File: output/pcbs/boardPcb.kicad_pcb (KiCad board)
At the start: 2 copper layers, 188.6 x 119.9 mm, 118 parts

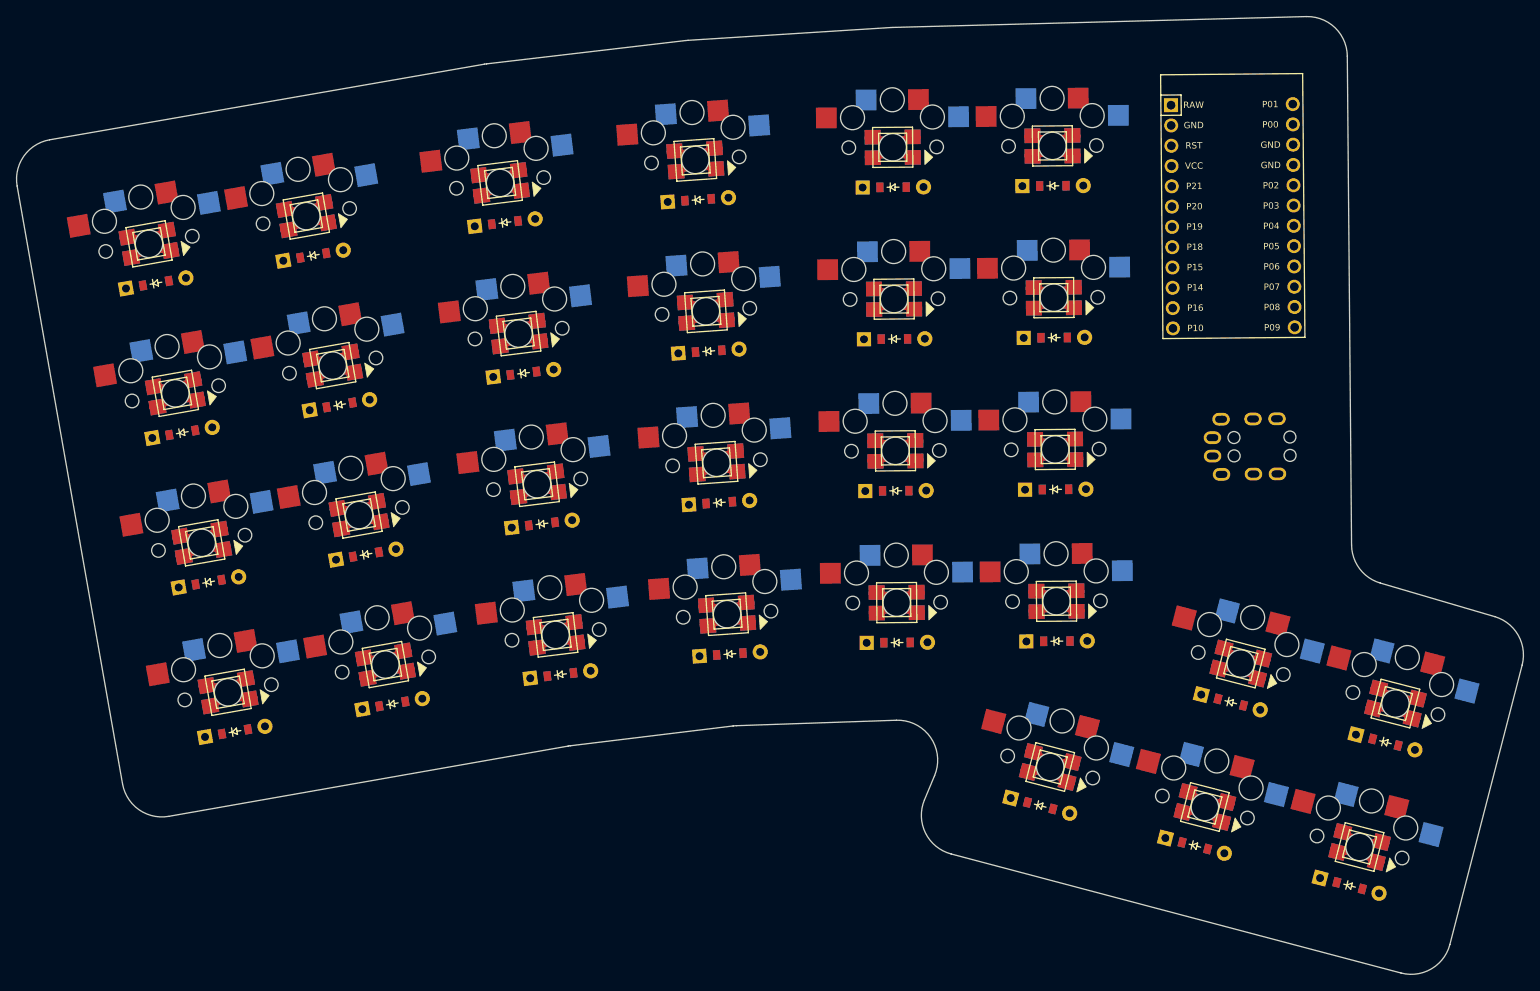
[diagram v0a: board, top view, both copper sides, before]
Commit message: created some PCB stuff; prep for layout
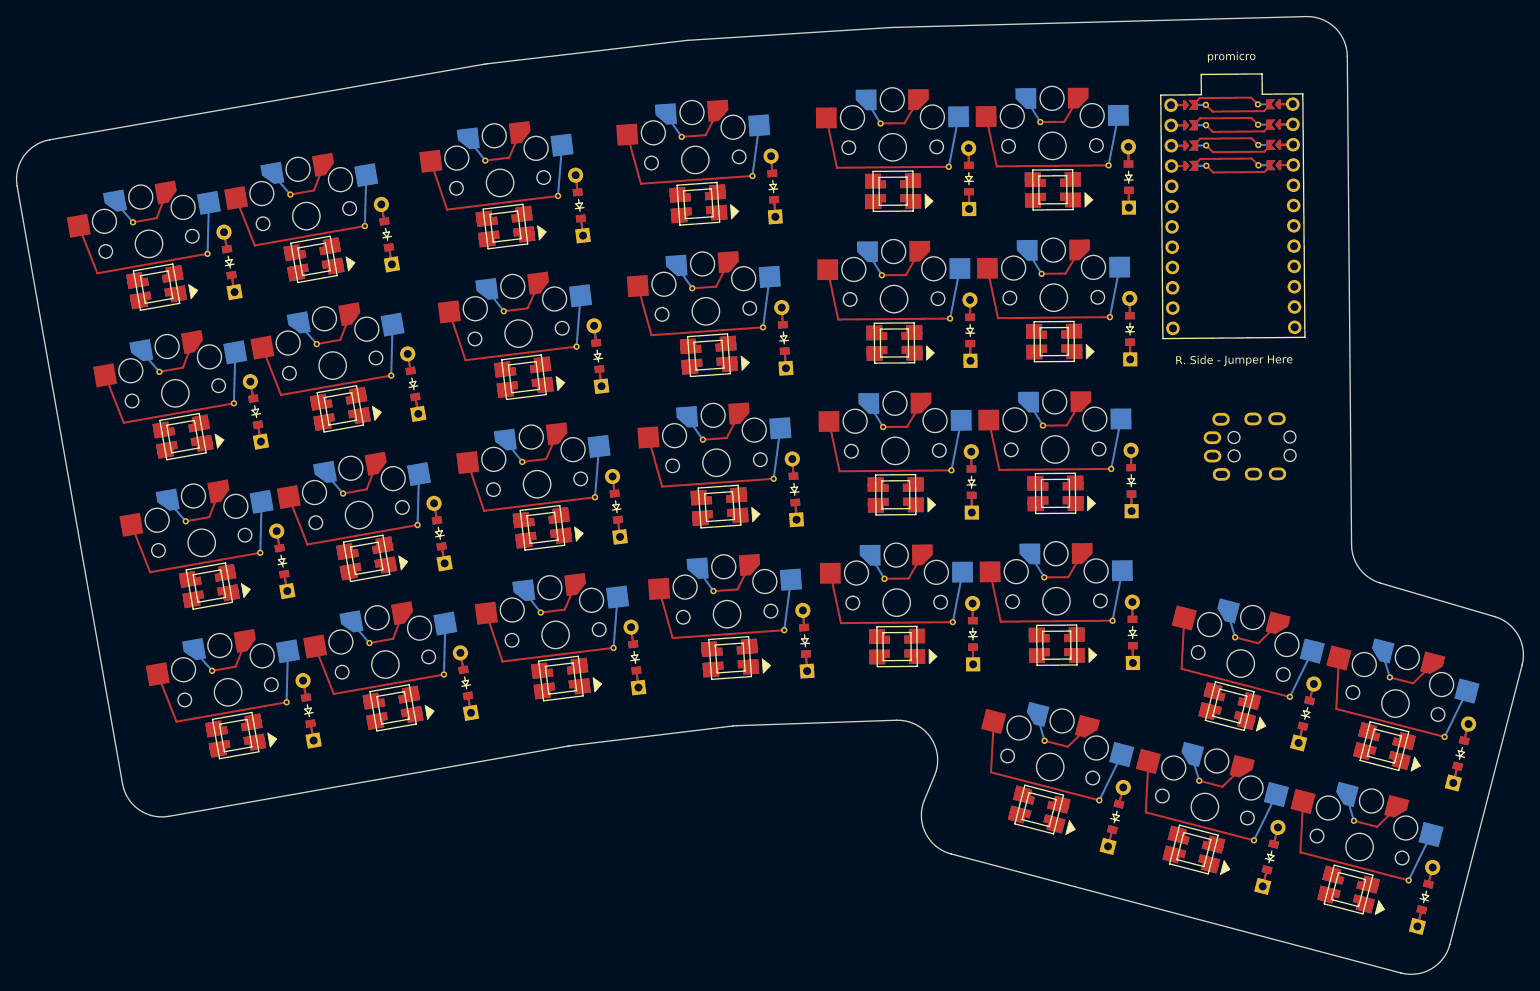
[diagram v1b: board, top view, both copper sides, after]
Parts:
- removed MCU1: , ProMicro
- added ?: , ProMicro, F.Cu at (258.8, 119.0)
- moved D1 9.55 mm to (143.1, 180.9), turned to 100 degrees
- moved D2 9.55 mm to (139.8, 162.2), turned to 100 degrees
- moved D4 9.55 mm to (133.2, 124.8), turned to 100 degrees
- moved D5 9.55 mm to (162.8, 177.4), turned to 100 degrees
- moved D6 9.55 mm to (159.5, 158.7), turned to 100 degrees
- moved D7 9.55 mm to (156.2, 140.0), turned to 100 degrees
- moved D8 9.55 mm to (152.9, 121.3), turned to 100 degrees
- moved D3 9.55 mm to (136.5, 143.5), turned to 100 degrees
- moved D10 9.55 mm to (181.6, 155.4), turned to 97 degrees
- moved D11 9.55 mm to (179.3, 136.5), turned to 97 degrees
- moved D12 9.55 mm to (177.0, 117.7), turned to 97 degrees
- moved D9 9.55 mm to (184.0, 174.2), turned to 97 degrees
- moved D25 9.55 mm to (244.1, 194.2), turned to 75.5 degrees
- moved D26 9.55 mm to (263.5, 199.2), turned to 75.5 degrees
- moved D27 9.55 mm to (282.9, 204.2), turned to 75.5 degrees
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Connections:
- D1 pad 1: (no net) -> P18
- D10 pad 1: (no net) -> P19
- D11 pad 1: (no net) -> P20
- D12 pad 1: (no net) -> P21
- D13 pad 1: (no net) -> P18
- D14 pad 1: (no net) -> P19
- D15 pad 1: (no net) -> P20
- D16 pad 1: (no net) -> P21
- D17 pad 1: (no net) -> P18
- D18 pad 1: (no net) -> P19
- D19 pad 1: (no net) -> P20
- D2 pad 1: (no net) -> P19
- D20 pad 1: (no net) -> P21
- D21 pad 1: (no net) -> P18
- D22 pad 1: (no net) -> P19
- D23 pad 1: (no net) -> P20
- D24 pad 1: (no net) -> P21
- D3 pad 1: (no net) -> P20
- D4 pad 1: (no net) -> P21
- D5 pad 1: (no net) -> P18
- D6 pad 1: (no net) -> P19
- D7 pad 1: (no net) -> P20
- D8 pad 1: (no net) -> P21
- D9 pad 1: (no net) -> P18
- LED1 pad 2: dout -> P7
- LED1 pad 22: dout -> P7
- LED1 pad 4: din -> P8
- LED1 pad 44: din -> P8
- LED10 pad 2: dout -> P7
- LED10 pad 22: dout -> P7
- LED10 pad 4: din -> P8
- LED10 pad 44: din -> P8
- LED11 pad 2: dout -> P7
- LED11 pad 22: dout -> P7
- LED11 pad 4: din -> P8
- LED11 pad 44: din -> P8
- LED12 pad 2: dout -> P7
- LED12 pad 22: dout -> P7
- LED12 pad 4: din -> P8
- LED12 pad 44: din -> P8
- LED13 pad 2: dout -> P7
- LED13 pad 22: dout -> P7
- LED13 pad 4: din -> P8
- LED13 pad 44: din -> P8
- LED14 pad 2: dout -> P7
- LED14 pad 22: dout -> P7
- LED14 pad 4: din -> P8
- LED14 pad 44: din -> P8
- LED15 pad 2: dout -> P7
- LED15 pad 22: dout -> P7
- LED15 pad 4: din -> P8
- LED15 pad 44: din -> P8
- LED16 pad 2: dout -> P7
- LED16 pad 22: dout -> P7
- LED16 pad 4: din -> P8
- LED16 pad 44: din -> P8
- LED17 pad 2: dout -> P7
- LED17 pad 22: dout -> P7
- LED17 pad 4: din -> P8
- LED17 pad 44: din -> P8
- LED18 pad 2: dout -> P7
- LED18 pad 22: dout -> P7
- LED18 pad 4: din -> P8
- LED18 pad 44: din -> P8
- LED19 pad 2: dout -> P7
- LED19 pad 22: dout -> P7
- LED19 pad 4: din -> P8
- LED19 pad 44: din -> P8
- LED2 pad 2: dout -> P7
- LED2 pad 22: dout -> P7
- LED2 pad 4: din -> P8
- LED2 pad 44: din -> P8
- LED20 pad 2: dout -> P7
- LED20 pad 22: dout -> P7
- LED20 pad 4: din -> P8
- LED20 pad 44: din -> P8
- LED21 pad 2: dout -> P7
- LED21 pad 22: dout -> P7
- LED21 pad 4: din -> P8
- LED21 pad 44: din -> P8
- LED22 pad 2: dout -> P7
- LED22 pad 22: dout -> P7
- LED22 pad 4: din -> P8
- LED22 pad 44: din -> P8
- LED23 pad 2: dout -> P7
- LED23 pad 22: dout -> P7
- LED23 pad 4: din -> P8
- LED23 pad 44: din -> P8
- LED24 pad 2: dout -> P7
- LED24 pad 22: dout -> P7
- LED24 pad 4: din -> P8
- LED24 pad 44: din -> P8
- LED25 pad 2: dout -> P7
- LED25 pad 22: dout -> P7
- LED25 pad 4: din -> P8
- LED25 pad 44: din -> P8
- LED26 pad 2: dout -> P7
- LED26 pad 22: dout -> P7
- LED26 pad 4: din -> P8
- LED26 pad 44: din -> P8
- LED27 pad 2: dout -> P7
- LED27 pad 22: dout -> P7
- LED27 pad 4: din -> P8
- LED27 pad 44: din -> P8
- LED28 pad 2: dout -> P7
- LED28 pad 22: dout -> P7
- LED28 pad 4: din -> P8
- LED28 pad 44: din -> P8
- LED29 pad 2: dout -> P7
- LED29 pad 22: dout -> P7
- LED29 pad 4: din -> P8
- LED29 pad 44: din -> P8
- LED3 pad 2: dout -> P7
- LED3 pad 22: dout -> P7
- LED3 pad 4: din -> P8
- LED3 pad 44: din -> P8
- LED30 pad 2: dout -> P7
- LED30 pad 22: dout -> P7
- LED30 pad 4: din -> P8
- LED30 pad 44: din -> P8
- LED31 pad 2: dout -> P7
- LED31 pad 22: dout -> P7
- LED31 pad 4: din -> P8
- LED31 pad 44: din -> P8
- LED32 pad 2: dout -> P7
- LED32 pad 22: dout -> P7
- LED32 pad 4: din -> P8
- LED32 pad 44: din -> P8
- LED33 pad 2: dout -> P7
- LED33 pad 22: dout -> P7
- LED33 pad 4: din -> P8
- LED33 pad 44: din -> P8
- LED34 pad 2: dout -> P7
- LED34 pad 22: dout -> P7
- LED34 pad 4: din -> P8
- LED34 pad 44: din -> P8
- LED35 pad 2: dout -> P7
- LED35 pad 22: dout -> P7
- LED35 pad 4: din -> P8
- LED35 pad 44: din -> P8
- LED36 pad 2: dout -> P7
- LED36 pad 22: dout -> P7
- LED36 pad 4: din -> P8
- LED36 pad 44: din -> P8
- LED37 pad 2: dout -> P7
- LED37 pad 22: dout -> P7
- LED37 pad 4: din -> P8
- LED37 pad 44: din -> P8
- LED38 pad 2: dout -> P7
- LED38 pad 22: dout -> P7
- LED38 pad 4: din -> P8
- LED38 pad 44: din -> P8
- LED39 pad 2: dout -> P7
- LED39 pad 22: dout -> P7
- LED39 pad 4: din -> P8
- LED39 pad 44: din -> P8
- LED4 pad 2: dout -> P7
- LED4 pad 22: dout -> P7
- LED4 pad 4: din -> P8
- LED4 pad 44: din -> P8
- LED40 pad 2: dout -> P7
- LED40 pad 22: dout -> P7
- LED40 pad 4: din -> P8
- LED40 pad 44: din -> P8
- LED41 pad 2: dout -> P7
- LED41 pad 22: dout -> P7
- LED41 pad 4: din -> P8
- LED41 pad 44: din -> P8
- LED42 pad 2: dout -> P7
- LED42 pad 22: dout -> P7
- LED42 pad 4: din -> P8
- LED42 pad 44: din -> P8
- LED43 pad 2: dout -> P7
- LED43 pad 22: dout -> P7
- LED43 pad 4: din -> P8
- LED43 pad 44: din -> P8
- LED44 pad 2: dout -> P7
- LED44 pad 22: dout -> P7
- LED44 pad 4: din -> P8
- LED44 pad 44: din -> P8
- LED45 pad 2: dout -> P7
- LED45 pad 22: dout -> P7
- LED45 pad 4: din -> P8
- LED45 pad 44: din -> P8
- LED46 pad 2: dout -> P7
- LED46 pad 22: dout -> P7
- LED46 pad 4: din -> P8
- LED46 pad 44: din -> P8
- LED47 pad 2: dout -> P7
- LED47 pad 22: dout -> P7
- LED47 pad 4: din -> P8
- LED47 pad 44: din -> P8
- LED48 pad 2: dout -> P7
- LED48 pad 22: dout -> P7
- LED48 pad 4: din -> P8
- LED48 pad 44: din -> P8
- LED49 pad 2: dout -> P7
- LED49 pad 22: dout -> P7
- LED49 pad 4: din -> P8
- LED49 pad 44: din -> P8
- LED5 pad 2: dout -> P7
- LED5 pad 22: dout -> P7
- LED5 pad 4: din -> P8
- LED5 pad 44: din -> P8
- LED50 pad 2: dout -> P7
- LED50 pad 22: dout -> P7
- LED50 pad 4: din -> P8
- LED50 pad 44: din -> P8
- LED51 pad 2: dout -> P7
- LED51 pad 22: dout -> P7
- LED51 pad 4: din -> P8
- LED51 pad 44: din -> P8
- LED52 pad 2: dout -> P7
- LED52 pad 22: dout -> P7
- LED52 pad 4: din -> P8
- LED52 pad 44: din -> P8
- LED53 pad 2: dout -> P7
- LED53 pad 22: dout -> P7
- LED53 pad 4: din -> P8
- LED53 pad 44: din -> P8
- LED54 pad 2: dout -> P7
- LED54 pad 22: dout -> P7
- LED54 pad 4: din -> P8
- LED54 pad 44: din -> P8
- LED55 pad 2: dout -> P7
- LED55 pad 22: dout -> P7
- LED55 pad 4: din -> P8
- LED55 pad 44: din -> P8
- LED56 pad 2: dout -> P7
- LED56 pad 22: dout -> P7
- LED56 pad 4: din -> P8
- LED56 pad 44: din -> P8
- LED57 pad 2: dout -> P7
- LED57 pad 22: dout -> P7
- LED57 pad 4: din -> P8
- LED57 pad 44: din -> P8
- LED58 pad 2: dout -> P7
- LED58 pad 22: dout -> P7
- LED58 pad 4: din -> P8
- LED58 pad 44: din -> P8
- LED6 pad 2: dout -> P7
- LED6 pad 22: dout -> P7
- LED6 pad 4: din -> P8
- LED6 pad 44: din -> P8
- LED7 pad 2: dout -> P7
- LED7 pad 22: dout -> P7
- LED7 pad 4: din -> P8
- LED7 pad 44: din -> P8
- LED8 pad 2: dout -> P7
- LED8 pad 22: dout -> P7
- LED8 pad 4: din -> P8
- LED8 pad 44: din -> P8
- LED9 pad 2: dout -> P7
- LED9 pad 22: dout -> P7
- LED9 pad 4: din -> P8
- LED9 pad 44: din -> P8
- S1 pad 1: (no net) -> P2
- S10 pad 1: (no net) -> P4
- S11 pad 1: (no net) -> P4
- S12 pad 1: (no net) -> P4
- S13 pad 1: (no net) -> P5
- S14 pad 1: (no net) -> P5
- S15 pad 1: (no net) -> P5
- S16 pad 1: (no net) -> P5
- S17 pad 1: (no net) -> P6
- S18 pad 1: (no net) -> P6
- S19 pad 1: (no net) -> P6
- S2 pad 1: (no net) -> P2
- S20 pad 1: (no net) -> P6
- S21 pad 1: (no net) -> P15
- S22 pad 1: (no net) -> P15
- S23 pad 1: (no net) -> P15
- S24 pad 1: (no net) -> P15
- S3 pad 1: (no net) -> P2
- S4 pad 1: (no net) -> P2
- S5 pad 1: (no net) -> P3
- S6 pad 1: (no net) -> P3
- S7 pad 1: (no net) -> P3
- S8 pad 1: (no net) -> P3
- S9 pad 1: (no net) -> P4
- TRRS1 pad 1: audioA -> GND
- TRRS1 pad 2: audioB -> P9
- TRRS1 pad 3: audioC -> P10
- TRRS1 pad 4: audioD -> VCC
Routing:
- net (no net): track 0.00 -> 1427.4 mm
